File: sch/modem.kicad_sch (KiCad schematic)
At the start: 48 parts, among them J10 TestPoint, J11 TestPoint, J12 TestPoint, J13 TestPoint, J14 TestPoint, J18 3V7_in, J4 EMPCB.SMAFSTJ.B.HT, J5 EMPCB.SMAFSTJ.B.HT, J6 TestPoint, J7 TestPoint, J8 TestPoint, J9 TestPoint, P1 SF72S006VBAR2500, U1 RC7620_1104625, U2 NX3008NBKW_115, U3 NX3008NBKW_115, U4 NX3008NBKW_115, U5 NX3008NBKW_115, U6 NX3008NBKW_115, U7 NX3008NBKW_115

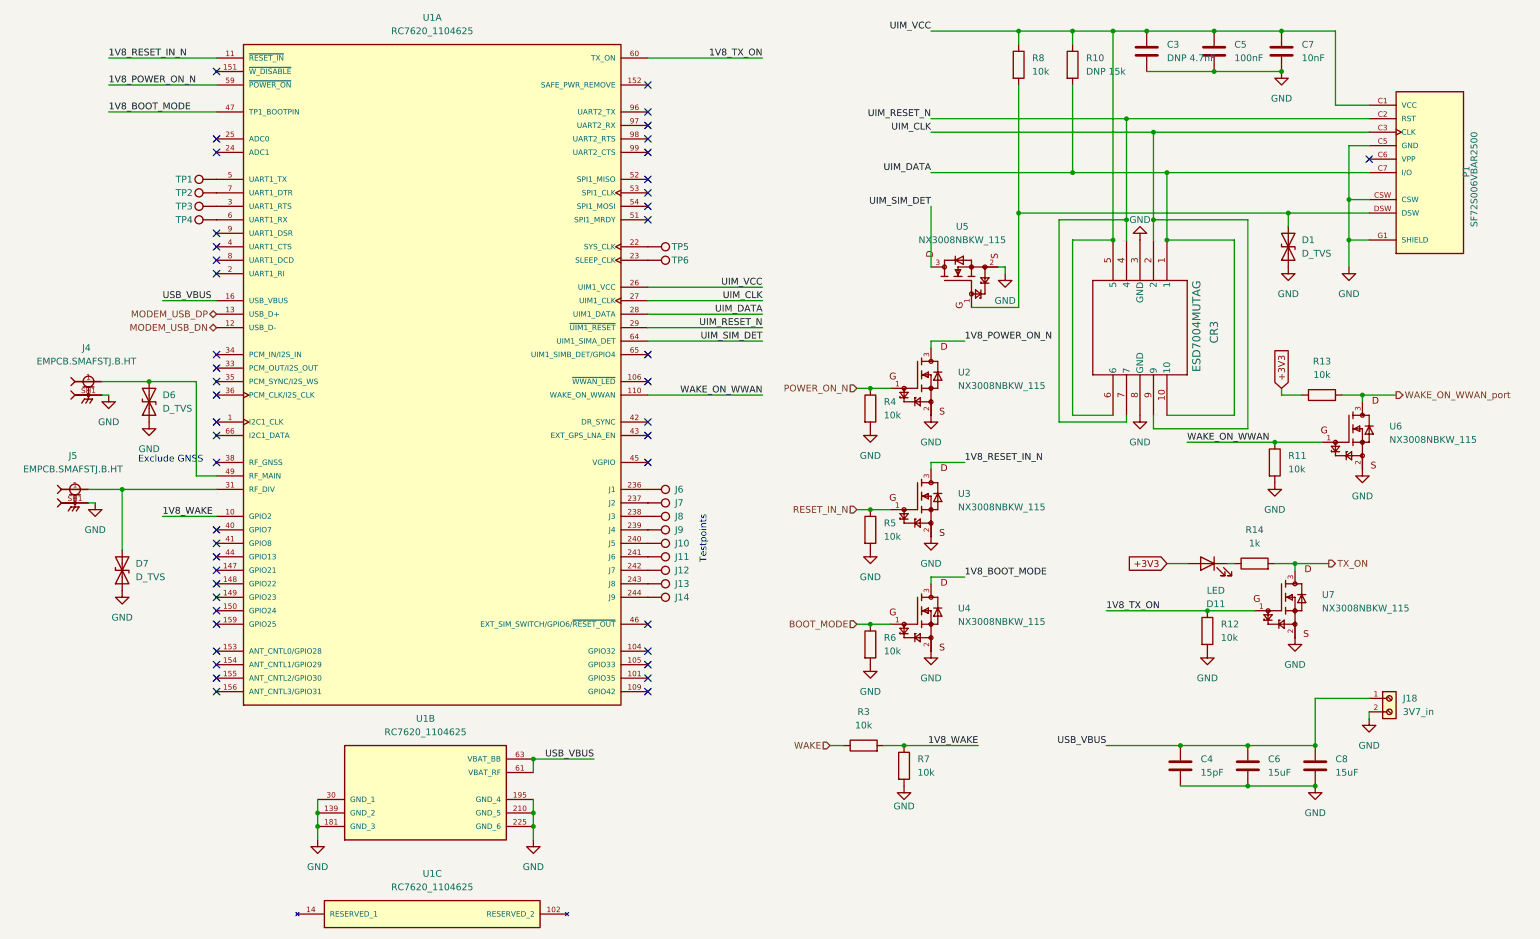
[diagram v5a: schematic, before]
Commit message: endret navn til redd delenummer for modem og simkort
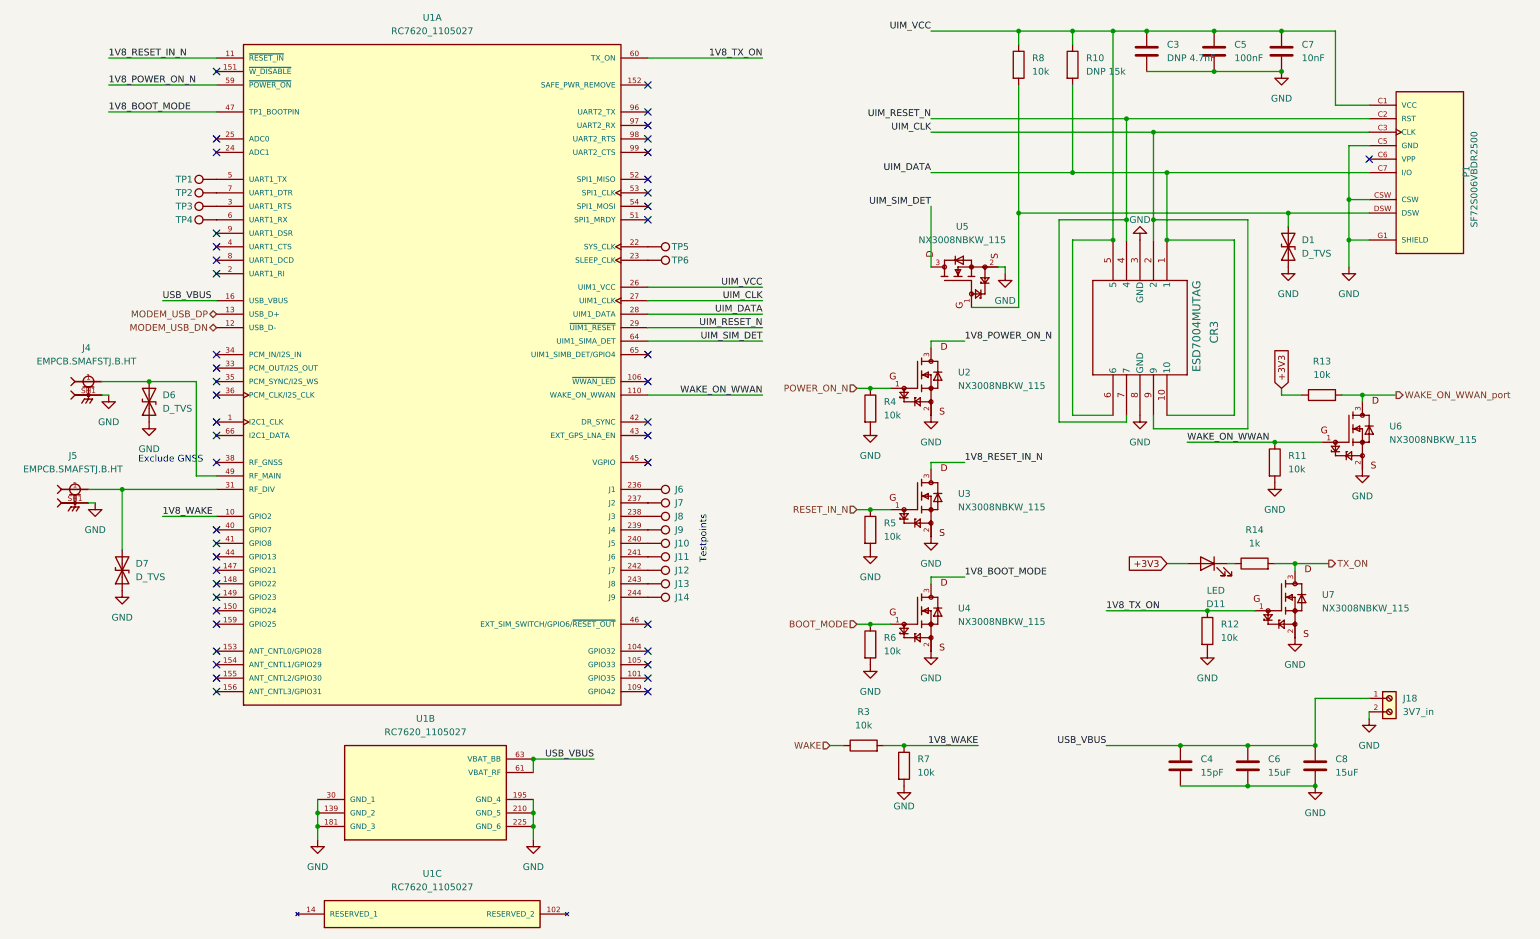
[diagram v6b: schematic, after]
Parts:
- P1: value SF72S006VBAR2500 -> SF72S006VBDR2500
- U1: value RC7620_1104625 -> RC7620_1105027
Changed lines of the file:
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@@
 			)
 		)
-		(property "Value" "SF72S006VBAR2500"
+		(property "Value" "SF72S006VBDR2500"
 			(at 280.67 44.4499 90)
 			(effects
@@
 			)
 		)
-		(property "Value" "RC7620_1104625"
+		(property "Value" "RC7620_1105027"
 			(at 85.09 16.51 0)
 			(effects
@@
 			)
 		)
-		(property "Value" "RC7620_1104625"
+		(property "Value" "RC7620_1105027"
 			(at 85.09 177.8 0)
 			(effects
@@
 			)
 		)
-		(property "Value" "RC7620_1104625"
+		(property "Value" "RC7620_1105027"
 			(at 83.82 148.59 0)
 			(effects

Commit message: pågebynt merging av pwr-supply og modem branches
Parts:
- removed C3: DNP 4.7nF, Capacitor_SMD:C_0603_1608Metric, symbol Device:C
- removed C4: 15pF, Capacitor_SMD:C_0603_1608Metric, symbol Device:C
- removed C5: 100nF, Capacitor_SMD:C_0603_1608Metric, symbol Device:C
- removed C6, C8: 15uF, Capacitor_SMD:C_0603_1608Metric, symbol Device:C
- removed C7: 10nF, Capacitor_SMD:C_0603_1608Metric, symbol Device:C
- removed CR3: ESD7004MUTAG, UDFN10_517BB_ONS, symbol ESD7004MUTAG:ESD7004MUTAG
- removed D11: LED, LTST-C190GKT:LEDM1608X80, symbol Device:LED
- removed D6, D7: D_TVS, Diode_SMD:D_0402_1005Metric, symbol Device:D_TVS
- removed J10, J11, J12, J13, J14, J6, J7, J8, J9: TestPoint, TestPoint:TestPoint_Loop_D2.50mm_Drill1.0mm, symbol Connector:TestPoint
- removed J18: 3V7_in, 691137710002:691137710002, symbol 691137710002:691137710002
- removed J4, J5: EMPCB.SMAFSTJ.B.HT, EMPCB.SMAFSTJ.B.HT:TAOGLAS_EMPCB.SMAFSTJ.B.HT, symbol EMPCB.SMAFSTJ.B.HT:EMPCB.SMAFSTJ.B.HT
- removed R10: DNP 15k, Resistor_SMD:R_0603_1608Metric, symbol Device:R
- removed R11, R12, R13, R3, R4, R5, R6, R7, R8: 10k, Resistor_SMD:R_0603_1608Metric, symbol Device:R
- removed R14: 1k, Resistor_SMD:R_0603_1608Metric, symbol Device:R
- removed TP1, TP2, TP3, TP4: T1, TestPoint:TestPoint_Loop_D2.50mm_Drill1.0mm, symbol Connector:TestPoint
- removed TP5, TP6: T1, TestPoint:TestPoint_Pad_D1.5mm, symbol Connector:TestPoint
- removed U1: RC7620_1105027, RC7620_1104625:XCVR_RC7620_1104625, symbol RC7620_1104625:RC7620_1104625
- removed U2, U3, U4, U5, U6, U7: NX3008NBKW_115, NX3008NBKW_115:SOT65P210X110-3N, symbol NX3008NBKW_115:NX3008NBKW_115
- added C38, C39: 220nF, Capacitor_SMD:C_0603_1608Metric, symbol Device:C
- added C40, C41, C42: 10pF, Capacitor_SMD:C_0603_1608Metric, symbol Device:C
- added C43: 100nF, Capacitor_SMD:C_0603_1608Metric, symbol Device:C
- added D3: LED, LTST-C190GKT:LEDM1608X80, symbol Device:LED
- added J10, J12, J15, J17: 20579-001E, 20579-001E:IPEX_20579-001E, symbol 20579-001E:20579-001E
- added J11, J13, J16, J18: 732511150, 732511150:CONN_73251-1150_MOL, symbol 732511150:732511150
- added J14: M.2_Socket_B, 2199119-3:TE_2199119-3, symbol 2199119-3:2199119-3
- added MP5, MP6: WA-SMSI_9774XXX243, WA-SMSI_9774XXX243:WA-SMSI_9774030243, symbol WA-SMSI_9774XXX243:WA-SMSI_9774XXX243
- added Q3: NX3008NBKW_115, NX3008NBKW_115:SOT65P210X110-3N, symbol NX3008NBKW_115:NX3008NBKW_115
- added R15, R17: 1k, Resistor_SMD:R_0603_1608Metric, symbol Device:R
- added R16: 100K, Resistor_SMD:R_0603_1608Metric, symbol Device:R
- added R18, R19, R20: 22, Resistor_SMD:R_0603_1608Metric, symbol Device:R
- added R21: 12.0 k, Resistor_SMD:R_0603_1608Metric, symbol Device:R
- added R22: 4.7K, Resistor_SMD:R_0603_1608Metric, symbol Device:R
- added T1, T2, T3, T4, T5: TestPoint, TestPoint:TestPoint_Loop_D2.60mm_Drill1.6mm_Beaded, symbol Connector:TestPoint
- added U9: ESD7004MUTAG, ESD7004MUTAG:UDFN10_517BB_ONS, symbol ESD7004MUTAG:ESD7004MUTAG
- renumbered D1 to D4
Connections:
- net GND: now also C40.2, C41.2, C42.2, C43.2, J10.G1, J10.G2, J10.G3, J11.2, J11.3, J12.G1, J12.G2, J12.G3, J13.2, J13.3, J14.11 (GND), J14.27 (GND), J14.3 (GND), J14.33 (GND), J14.39 (GND), J14.45 (GND), J14.5 (GND), J14.51 (GND), J14.57 (GND), J14.69 (CONFIG_1), J14.71 (GND), J14.73 (GND), J15.G1, J15.G2, J15.G3, J16.2, J16.3, J17.G1, J17.G2, J17.G3, J18.2, J18.3, MP5.1, MP6.1, Q3.2, R16.2, R22.2, U9.3 (GND), U9.8 (GND); no longer P1.CSW
- net MODEM_USB_DN: now also J14.9 (USB_DM)
- net MODEM_USB_DP: now also J14.7 (USB_DP)
- net USIM1_DET: now reaches D4.2 (A2), P1.DSW
- net USIM1_DET: now also J14.66 (USIM1_DET), T1.1
- net UIM_CLK: no longer names the net of P1.C3 (CLK)
- net UIM_CLK: now also C41.1, R19.2, T3.1, U9.4, U9.7
- net UIM_DATA: no longer names the net of P1.C7 (I/O)
- net UIM_DATA: now also C40.1, R20.2, R21.1, T2.1, U9.5, U9.6
- net UIM_RESET_N: no longer names the net of P1.C2 (RST)
- net UIM_RESET_N: now also C42.1, R18.2, T4.1, U9.2, U9.9
- net UIM_VCC renamed USIM1_VDD
- net USIM1_VDD: now also C43.1, J14.36 (USIM1_VDD), R21.2, T5.1, U9.1, U9.10
- new net: P1.CSW, R22.1
- new net: J10.1, J11.1
- new net: J15.1, J16.1
- new net: J12.1, J13.1
- new net: C38.2, J14.47 (PCIE_RX_M)
- new net: Q3.1, R15.2, R16.1
- new net: C39.2, J14.49 (PCIE_RX_P)
- new net: D3.1, J14.10 (LED_WWAN)
- new net: D3.2, R17.2
- new net: J17.1, J18.1
- new net: J14.SH1 (SHIELD), J14.SH2 (SHIELD)
- new net +3V5: J14.2 (VCC), J14.4 (VCC), J14.70 (VCC), J14.72 (VCC), J14.74 (VCC), R17.1
- new net MODEM_RESET_N: R15.1
- new net MODEM_USB_RX_N: J14.35 (USB_RX_M)
- new net MODEM_USB_RX_P: J14.37 (USB_RX_P)
- new net MODEM_USB_TX_N: J14.29 (USB_TX_M)
- new net MODEM_USB_TX_P: J14.31 (USB_TX_P)
- new net PCIE_CLK_N: J14.53 (PCIE_REFCLK_M)
- new net PCIE_CLK_P: J14.55 (PCIE_REFCLK_P)
- new net PCIE_PWR_EN: J14.6 (FULL_POWER_OFF)
- new net PCIE_RX_N: J14.41 (PCIE_TX_M)
- new net PCIE_RX_P: J14.43 (PCIE_TX_P)
- new net PCIE_TX_N: C38.1
- new net PCIE_TX_P: C39.1
- new net PCIE_nCLKREQ: J14.52 (PCIE_CLKREQ)
- new net PCIE_nRST: J14.50 (PCIE_RST_N)
- new net PCIE_nWAKE: J14.54 (PCIE_WAKE)
- new net RESET: J14.67 (RESET), Q3.3
- new net USIM1_CLK: J14.32 (USIM1_CLK), R19.1
- new net USIM1_DATA: J14.34 (USIM1_DATA), R20.1
- new net USIM1_RST: J14.30 (USIM1_RST), R18.1
- new net WAKE_ON_WAN: J14.23 (WAKE_ON_WAN)
- no-connect marks 46 -> 27
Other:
- note added: "10-20k, chose 12 bc we already use one"
- note added: "Activity LED"
- note added: "Airplane mode"
- note added: "CD1"
- note added: "CD2"
- note added: "Disable GNSS"
- note added: "M.2 Standoffs"
- note added: "MHF4L Connector Receptacle"
- note added: "Molex SMA RCPT edge mnt"
- note removed: "Exclude GNSS"
- note removed: "Testpoints"
- moved on the sheet: D4, P1

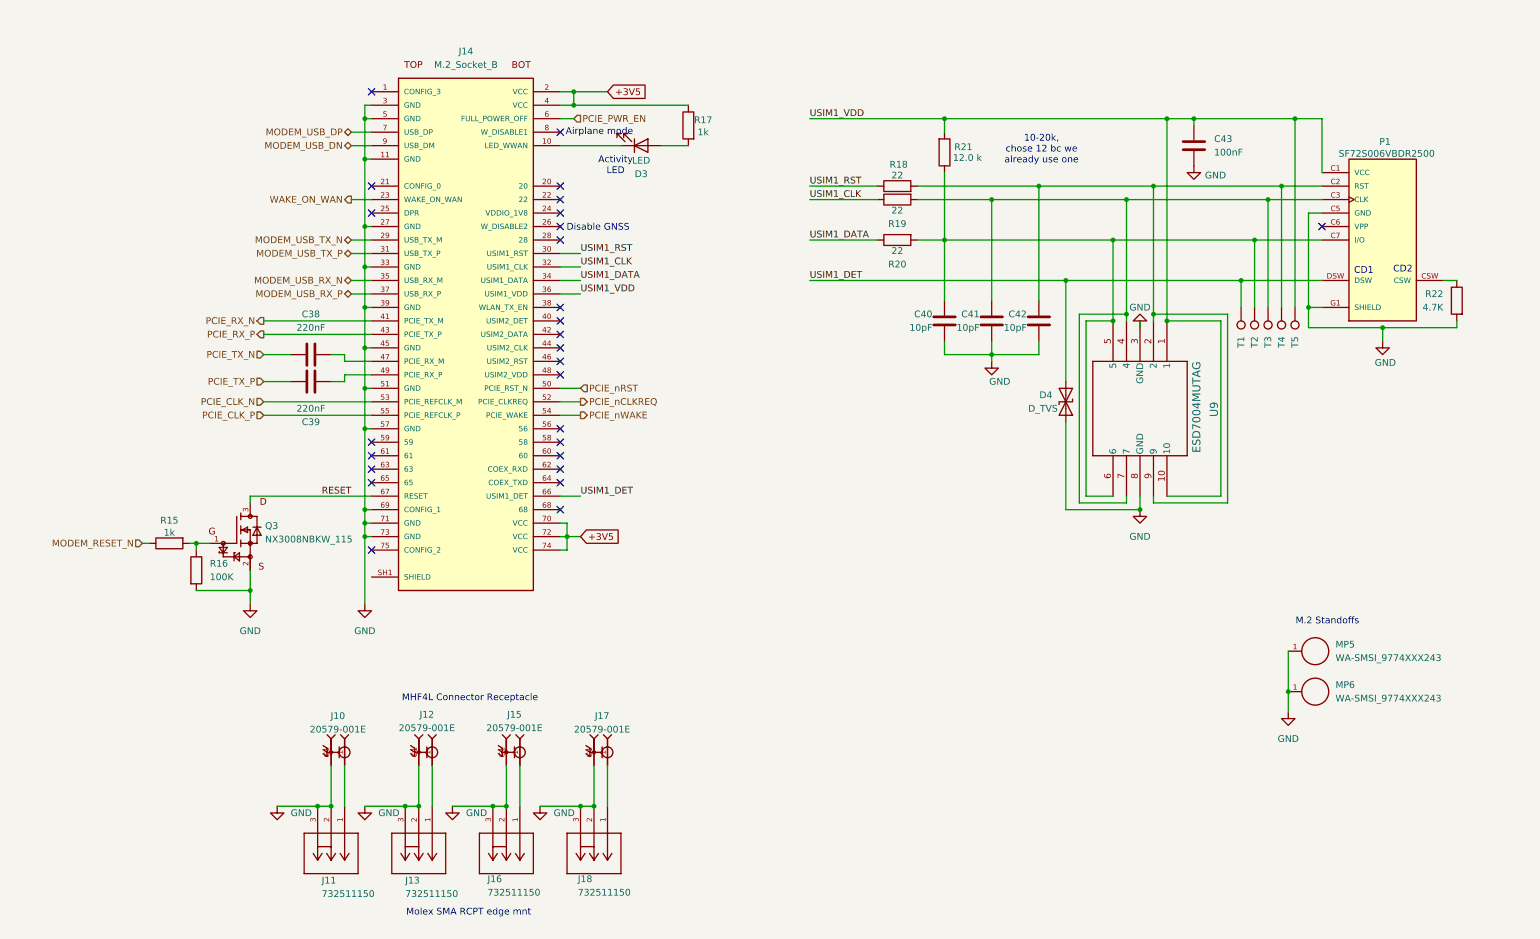
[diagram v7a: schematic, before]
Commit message: lagt inn footprint på alt, obs feil footprint i pwr-supply
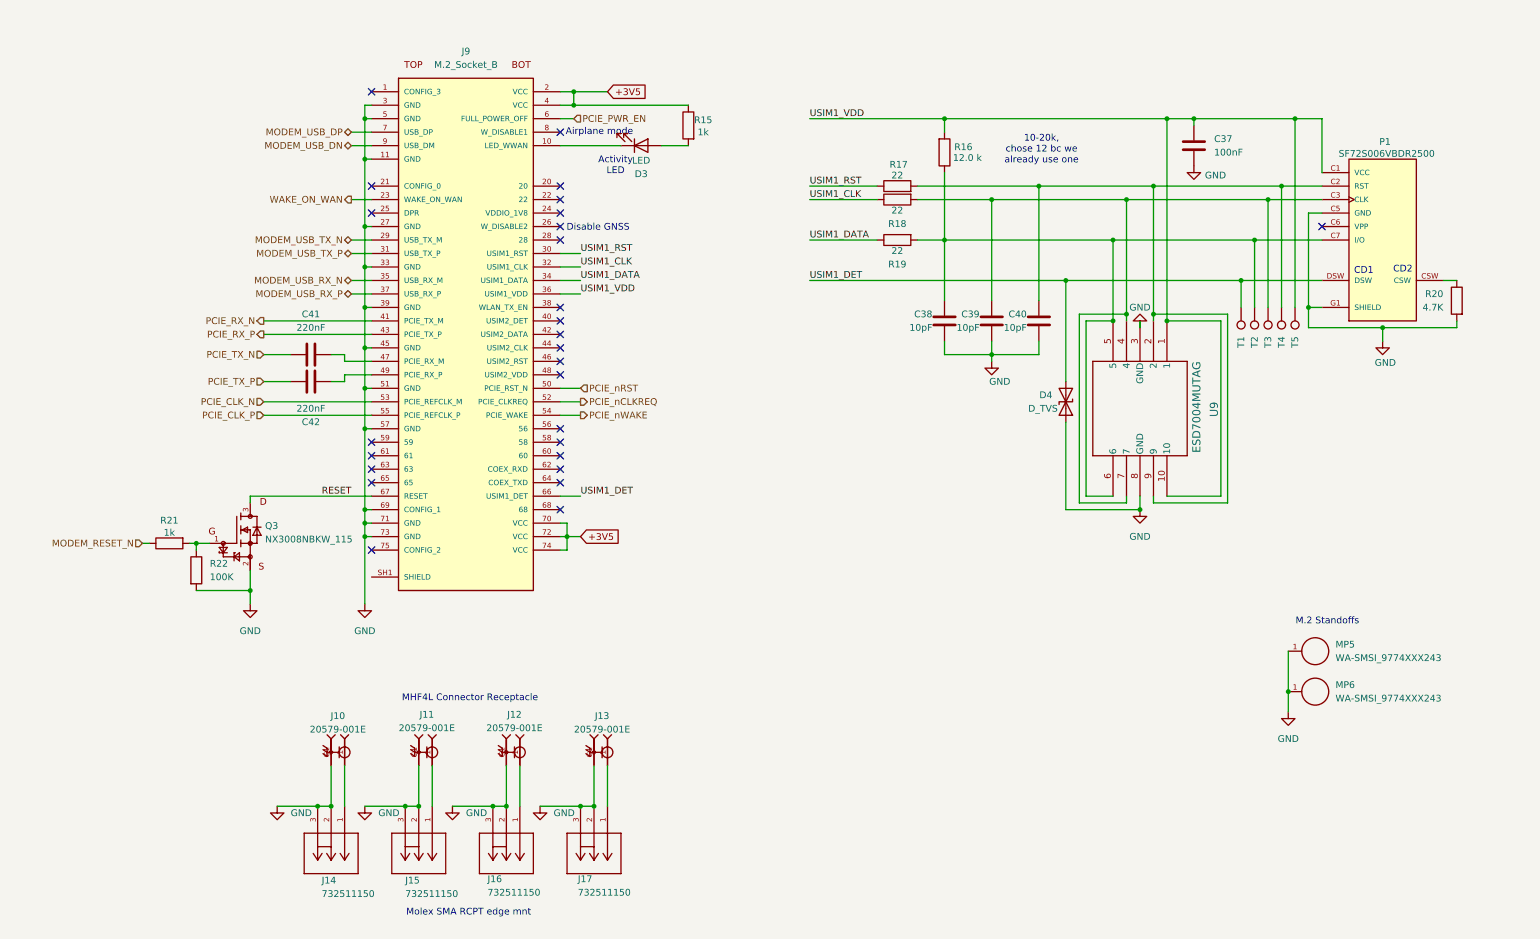
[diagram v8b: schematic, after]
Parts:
- renumbered C43 to C37, C40 to C38, C41 to C39, C42 to C40, C38 to C41, C39 to C42, J12 to J11, J15 to J12, J17 to J13, J11 to J14, J13 to J15, J18 to J17, J14 to J9, R17 to R15, R21 to R16, R18 to R17, R19 to R18, R20 to R19, R22 to R20, R15 to R21, R16 to R22
